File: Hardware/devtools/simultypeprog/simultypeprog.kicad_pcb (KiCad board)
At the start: 2 copper layers, 30.7 x 58.2 mm, 11 parts, among them J2 Conn_01x07, J3 Conn_01x07, SW1 SW_Push

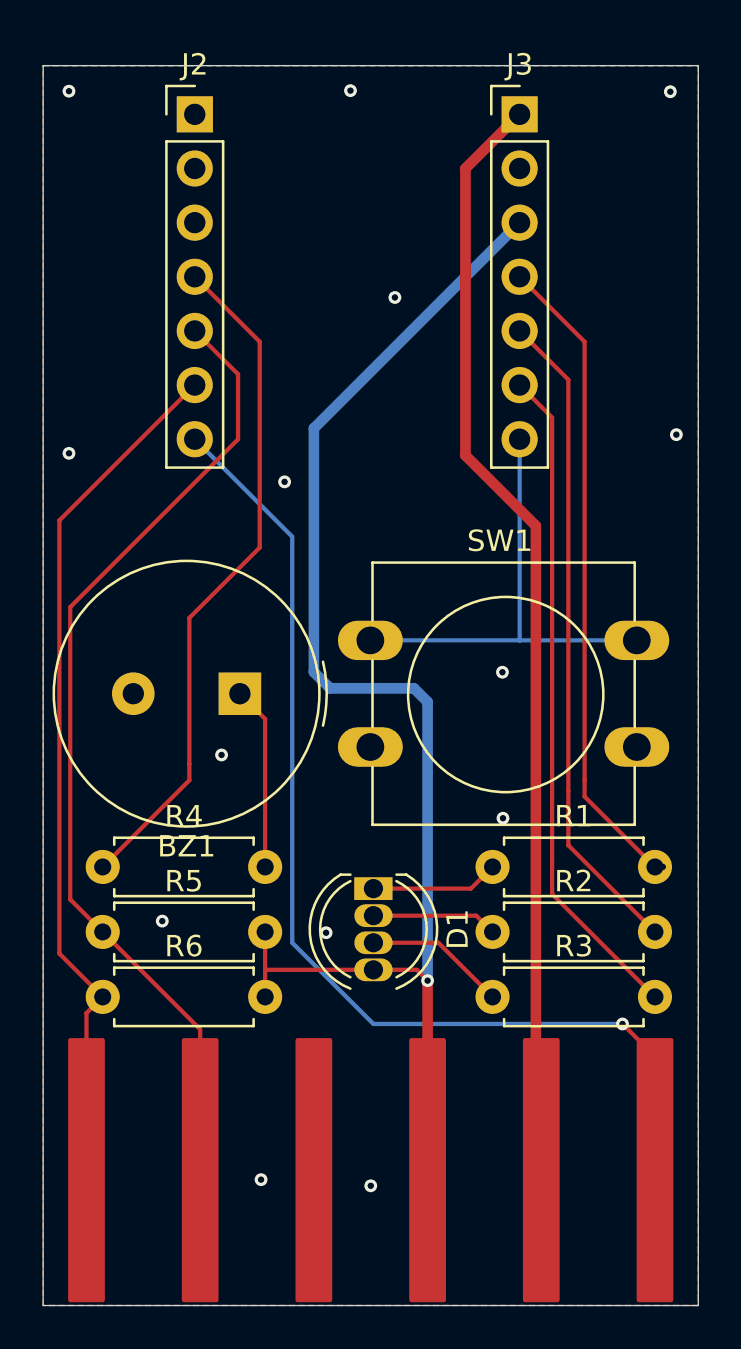
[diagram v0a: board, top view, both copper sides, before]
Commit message: Minor graphics cleanup
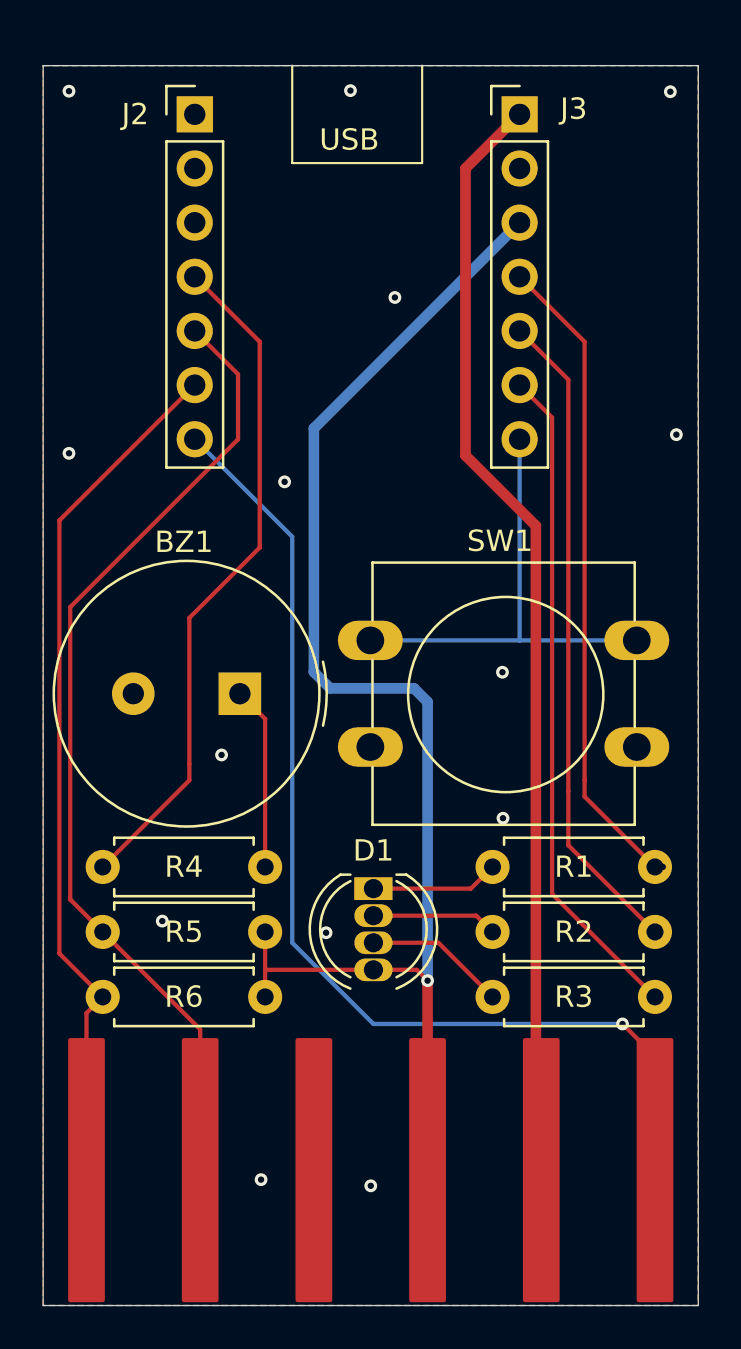
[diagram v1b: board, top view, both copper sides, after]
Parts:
- added J1: Conn_01x01, Connector_Wire:SolderWirePad_1x01_SMD_1x2mm, F.Cu at (109.0, 97.8)
- added J4: Conn_01x01, Connector_Wire:SolderWirePad_1x01_SMD_1x2mm, F.Cu at (103.6, 97.8)
- added J5: Conn_01x01, Connector_Wire:SolderWirePad_1x01_SMD_1x2mm, F.Cu at (114.3, 97.8)
- added J6: Conn_01x01, Connector_Wire:SolderWirePad_1x01_SMD_1x2mm, F.Cu at (119.6, 97.8)
- added J7: Conn_01x01, Connector_Wire:SolderWirePad_1x01_SMD_1x2mm, F.Cu at (125.0, 97.8)
- added J8: Conn_01x01, Connector_Wire:SolderWirePad_1x01_SMD_1x2mm, F.Cu at (130.3, 97.8)
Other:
- board text added: "USB"
